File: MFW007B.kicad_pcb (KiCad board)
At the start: 4 copper layers, 84 x 42 mm, 98 parts, among them J1 Conn_01x04, J2 Conn_02x07, J3 4P JST-SH, J4 Conn_02x03, SW2 SW_Push, SW3 SW_Push, SW4 SW_Push, U1 24AA02-OT, U2 W5500, U3 STM32F103C8T6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

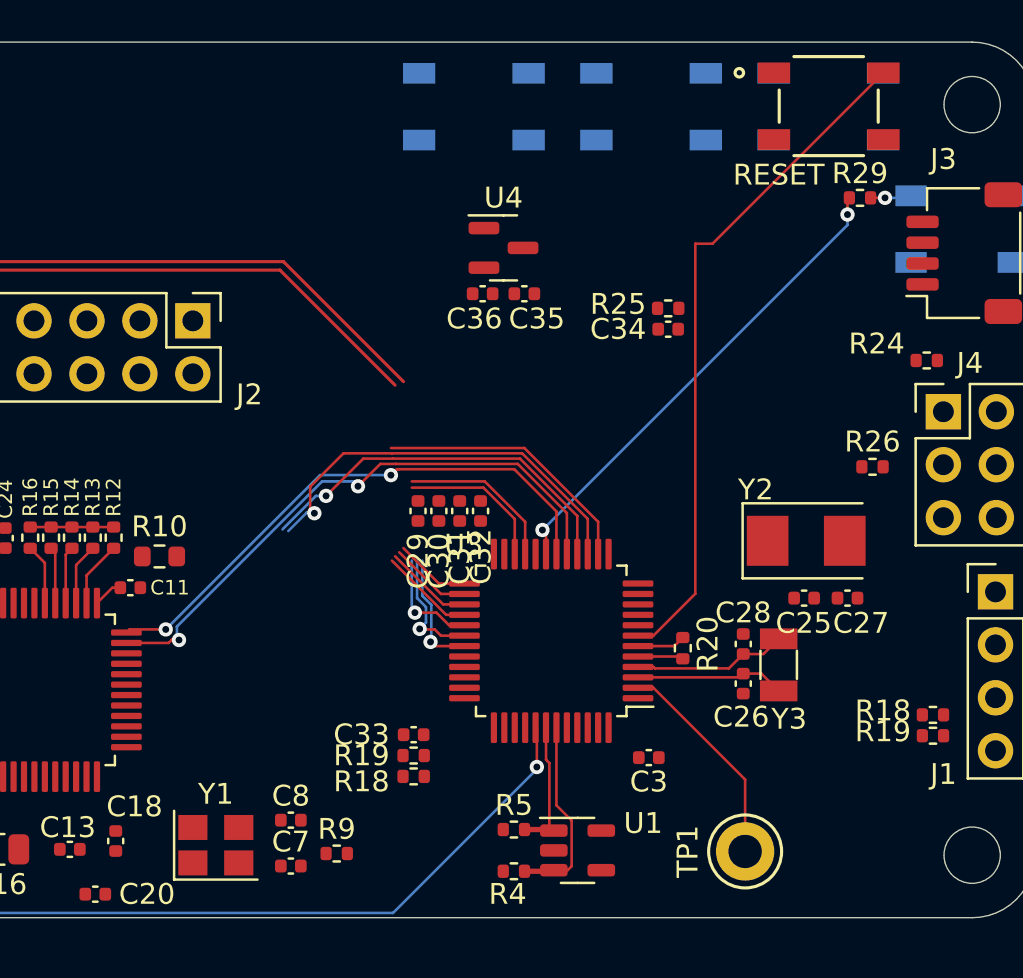
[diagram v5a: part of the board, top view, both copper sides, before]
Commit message: rotate mcu
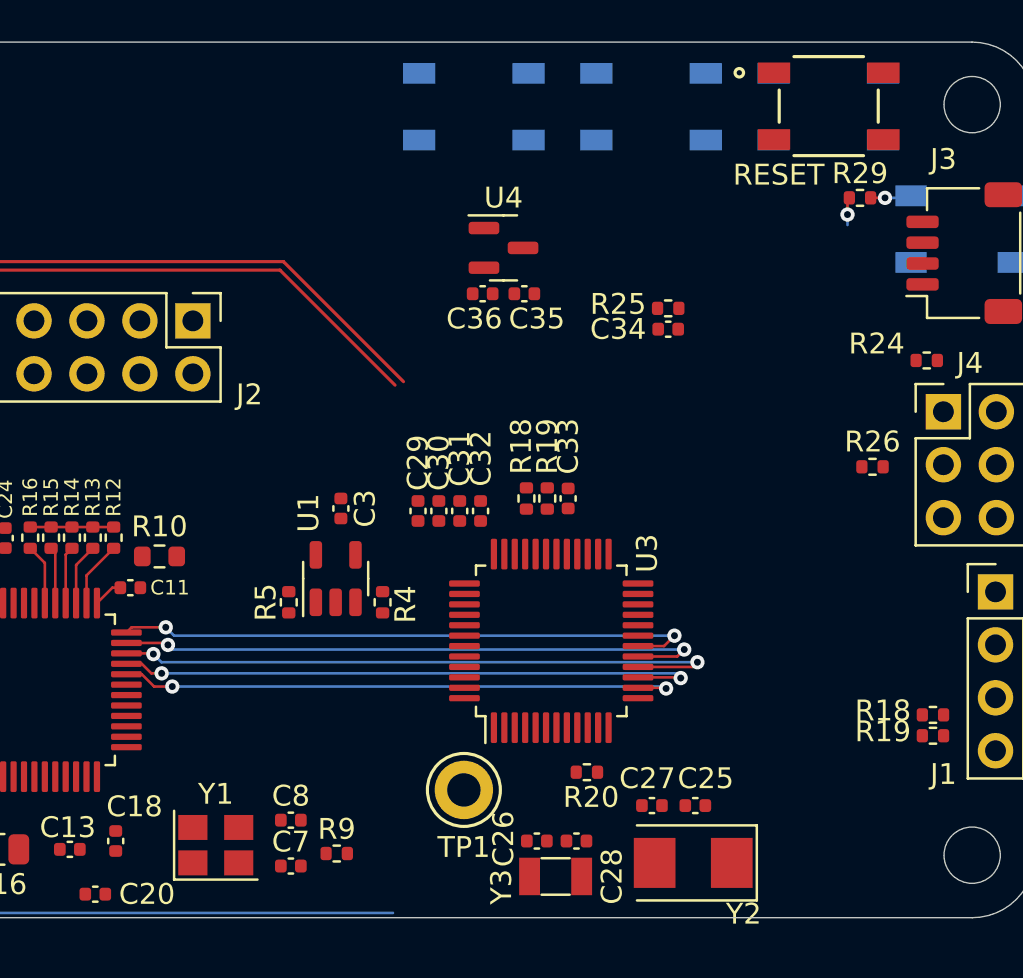
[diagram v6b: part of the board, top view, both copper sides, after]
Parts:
- moved C3 19.0 mm to (139.1, 101.5), turned to -90 degrees
- moved U1 17.5 mm to (138.8, 104.9), turned to 90 degrees
- moved Y2 16.4 mm to (156.0, 118.5), turned to 180 degrees
- moved R5 15.3 mm to (136.6, 106.0), turned to -90 degrees
- moved Y3 14.7 mm to (149.4, 119.2), turned to 0 degrees
- moved R18 14.4 mm to (148.0, 101.0), turned to 90 degrees
- moved R4 14.4 mm to (141.1, 106.0), turned to -90 degrees
- moved R19 13.9 mm to (149.0, 101.0), turned to -90 degrees
- moved TP1 13.8 mm to (145.0, 115.0), turned to 180 degrees
- moved C27 13.7 mm to (154.0, 115.8), turned to 180 degrees
- moved C33 13.5 mm to (150.0, 101.0), turned to -90 degrees
- moved C26 12.5 mm to (148.5, 117.5), turned to 180 degrees
- moved C28 12.4 mm to (150.4, 117.5), turned to 0 degrees
- moved C25 11.2 mm to (156.1, 115.8), turned to 180 degrees
- moved R20 7.52 mm to (150.9, 114.2), turned to 0 degrees
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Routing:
- net /RESET_SW: track 32.8 -> 0.00 mm
- net /RGB_LED: track 23.3 -> 1.34 mm, vias 2 -> 1
- net /Ethernet MAC PHY/CS: track 13.0 -> 27.5 mm, vias 0 -> 2
- net /Ethernet MAC PHY/MISO: track 18.5 -> 30.5 mm, vias 1 -> 2
- net /NTP_LED: track 61.3 -> 49.6 mm, vias 2 -> 1
- net Net-(TP1-Pad1): track 10.4 -> 0.00 mm
- net /I2C1_SDA: track 9.31 -> 0.00 mm
- net /Ethernet MAC PHY/SCLK: track 19.9 -> 28.9 mm, vias 1 -> 2
- net /I2C2_SCL: track 7.79 -> 0.00 mm
- net /MCU/OSC32_OUT: track 7.37 -> 0.00 mm
- net /I2C2_SDA: track 7.25 -> 0.00 mm
- net /MCU/OSC32_IN: track 7.17 -> 0.00 mm
- net /I2C1_SCL: track 6.52 -> 0.00 mm
- net /USER_SW_2: track 5.86 -> 0.00 mm, vias 1 -> 0
- net /USER_SW_3: track 5.80 -> 0.00 mm, vias 1 -> 0
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
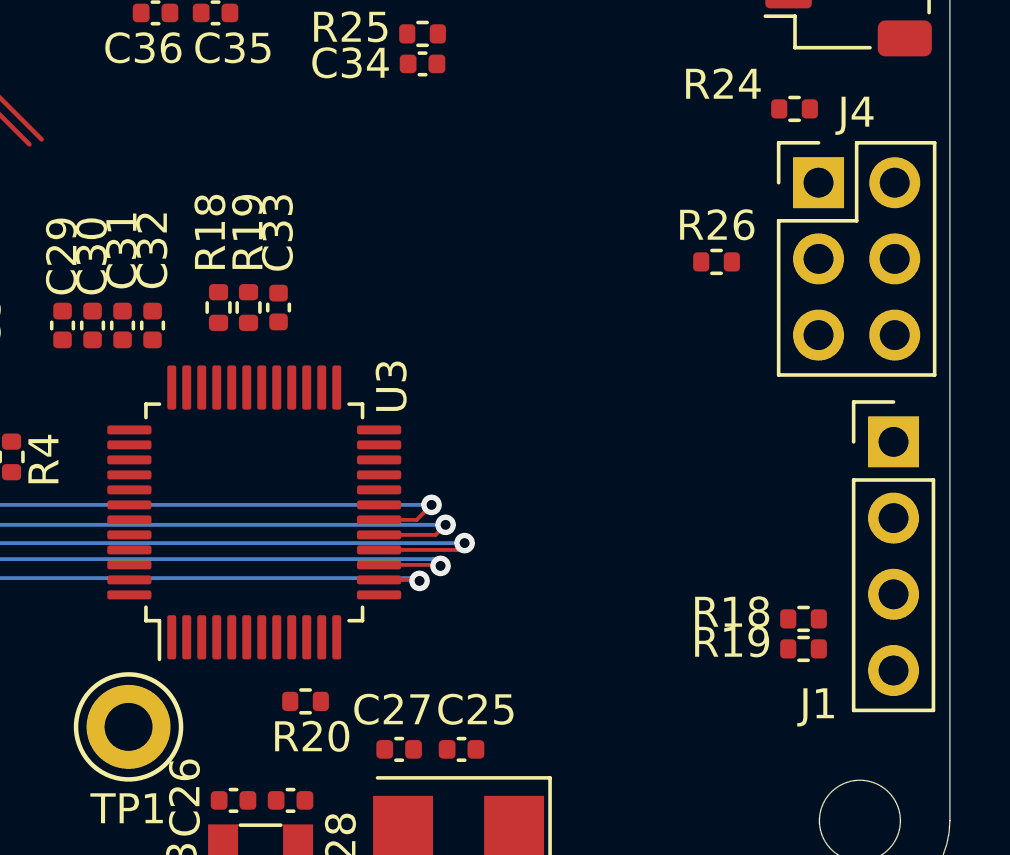
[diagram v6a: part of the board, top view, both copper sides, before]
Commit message: remove duplicate components
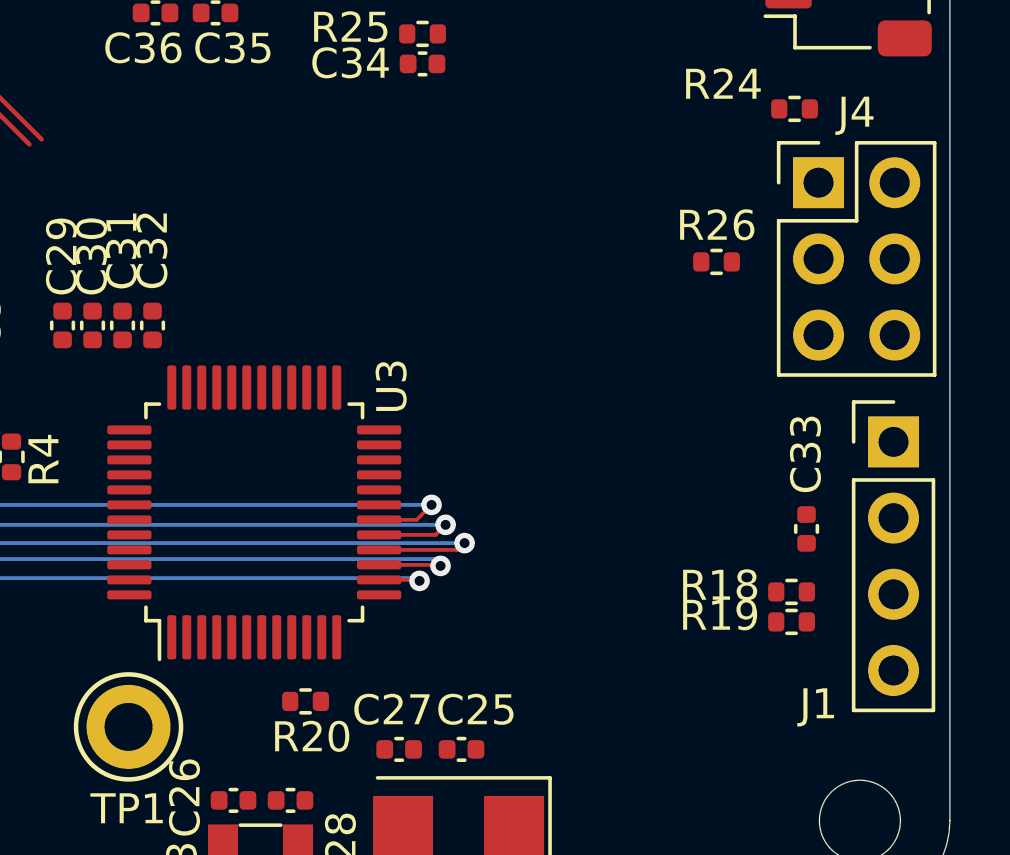
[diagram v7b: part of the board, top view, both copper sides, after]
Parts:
- removed the R18 at (148.0, 101.0)
- removed the R19 at (149.0, 101.0)
- moved C33 19.1 mm to (167.6, 108.4)
- moved R18 0.98 mm to (167.1, 110.5)
- moved R19 0.98 mm to (167.1, 111.5)
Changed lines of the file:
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@@
   )
   (footprint "Resistor_SMD:R_0402_1005Metric" (layer "F.Cu")
-    (at 167.5 111.4 180)
+    (at 167.1 110.5 180)
     (descr "Resistor SMD 0402 (1005 Metric), square (rectangular) end terminal, IPC_7351 nominal, (Body size source: IPC-SM-782 page 72, https://www.pcb-3d.com/wordpress/wp-content/uploads/ipc-sm-782a_amendment_1_and_2.pdf), generated with kicad-footprint-generator")
     (tags "resistor")
@@
   )
   (footprint "Capacitor_SMD:C_0402_1005Metric" (layer "F.Cu")
-    (at 150 101.02 -90)
+    (at 167.6 108.4 -90)
     (descr "Capacitor SMD 0402 (1005 Metric), square (rectangular) end terminal, IPC_7351 nominal, (Body size source: IPC-SM-782 page 76, https://www.pcb-3d.com/wordpress/wp-content/uploads/ipc-sm-782a_amendment_1_and_2.pdf), generated with kicad-footprint-generator")
     (tags "capacitor")
@@
     (pad "2" smd roundrect (at 0.51 0 180) (locked) (size 0.54 0.64) (layers "F.Cu" "F.Paste" "F.Mask") (roundrect_rratio 0.25)
       (net 74 "/MCU/BOOT1"))
-    (model "${KICAD6_3DMODEL_DIR}/Resistor_SMD.3dshapes/R_0402_1005Metric.wrl"
-      (offset (xyz 0 0 0))
-      (scale (xyz 1 1 1))
-      (rotate (xyz 0 0 0))
-    )
-  )
-  (footprint "Resistor_SMD:R_0402_1005Metric" (layer "F.Cu")
-    (at 149 101.02 -90)
-    (descr "Resistor SMD 0402 (1005 Metric), square (rectangular) end terminal, IPC_7351 nominal, (Body size source: IPC-SM-782 page 72, https://www.pcb-3d.com/wordpress/wp-content/uploads/ipc-sm-782a_amendment_1_and_2.pdf), generated with kicad-footprint-generator")
-    (tags "resistor")
-    (property "Sheet file" "mcu.kicad_sch")
-    (property "Sheet name" "MCU")
-    (attr smd)
-    (fp_text reference "R19" (at -2.5 0 90) (layer "F.SilkS")
-      (effects (font (size 1 1) (thickness 0.15)))
-    )
-    (fp_text value "10K" (at -2.25 1.25 90) (layer "F.Fab")
-      (effects (font (size 1 1) (thickness 0.15)))
-    )
-    (fp_text user "${REFERENCE}" (at 0 0 90) (layer "F.Fab")
-      (effects (font (size 0.26 0.26) (thickness 0.04)))
-    )
-    (fp_line (start -0.153641 0.38) (end 0.153641 0.38) (layer "F.SilkS") (width 0.12))
-    (fp_line (start -0.153641 -0.38) (end 0.153641 -0.38) (layer "F.SilkS") (width 0.12))
-    (fp_line (start 0.93 -0.47) (end 0.93 0.47) (layer "F.CrtYd") (width 0.05))
-    (fp_line (start 0.93 0.47) (end -0.93 0.47) (layer "F.CrtYd") (width 0.05))
-    (fp_line (start -0.93 -0.47) (end 0.93 -0.47) (layer "F.CrtYd") (width 0.05))
-    (fp_line (start -0.93 0.47) (end -0.93 -0.47) (layer "F.CrtYd") (width 0.05))
-    (fp_line (start 0.525 -0.27) (end 0.525 0.27) (layer "F.Fab") (width 0.1))
-    (fp_line (start 0.525 0.27) (end -0.525 0.27) (layer "F.Fab") (width 0.1))
-    (fp_line (start -0.525 -0.27) (end 0.525 -0.27) (layer "F.Fab") (width 0.1))
-    (fp_line (start -0.525 0.27) (end -0.525 -0.27) (layer "F.Fab") (width 0.1))
-    (pad "1" smd roundrect (at -0.51 0 270) (locked) (size 0.54 0.64) (layers "F.Cu" "F.Paste" "F.Mask") (roundrect_rratio 0.25)
-      (net 3 "+3V3"))
-    (pad "2" smd roundrect (at 0.51 0 270) (locked) (size 0.54 0.64) (layers "F.Cu" "F.Paste" "F.Mask") (roundrect_rratio 0.25)
-      (net 23 "/MCU/SWCLK"))
     (model "${KICAD6_3DMODEL_DIR}/Resistor_SMD.3dshapes/R_0402_1005Metric.wrl"
       (offset (xyz 0 0 0))
@@
     )
   )
-  (footprint "Resistor_SMD:R_0402_1005Metric" (layer "F.Cu")
-    (at 148 101.02 90)
-    (descr "Resistor SMD 0402 (1005 Metric), square (rectangular) end terminal, IPC_7351 nominal, (Body size source: IPC-SM-782 page 72, https://www.pcb-3d.com/wordpress/wp-content/uploads/ipc-sm-782a_amendment_1_and_2.pdf), generated with kicad-footprint-generator")
-    (tags "resistor")
-    (property "Sheet file" "mcu.kicad_sch")
-    (property "Sheet name" "MCU")
-    (attr smd)
-    (fp_text reference "R18" (at 2.5 -0.25 90) (layer "F.SilkS")
-      (effects (font (size 1 1) (thickness 0.15)))
-    )
-    (fp_text value "10K" (at 2.25 1 90) (layer "F.Fab")
-      (effects (font (size 1 1) (thickness 0.15)))
-    )
-    (fp_text user "${REFERENCE}" (at 0 0 90) (layer "F.Fab")
-      (effects (font (size 0.26 0.26) (thickness 0.04)))
-    )
-    (fp_line (start -0.153641 -0.38) (end 0.153641 -0.38) (layer "F.SilkS") (width 0.12))
-    (fp_line (start -0.153641 0.38) (end 0.153641 0.38) (layer "F.SilkS") (width 0.12))
-    (fp_line (start -0.93 0.47) (end -0.93 -0.47) (layer "F.CrtYd") (width 0.05))
-    (fp_line (start 0.93 -0.47) (end 0.93 0.47) (layer "F.CrtYd") (width 0.05))
-    (fp_line (start -0.93 -0.47) (end 0.93 -0.47) (layer "F.CrtYd") (width 0.05))
-    (fp_line (start 0.93 0.47) (end -0.93 0.47) (layer "F.CrtYd") (width 0.05))
-    (fp_line (start 0.525 0.27) (end -0.525 0.27) (layer "F.Fab") (width 0.1))
-    (fp_line (start -0.525 -0.27) (end 0.525 -0.27) (layer "F.Fab") (width 0.1))
-    (fp_line (start 0.525 -0.27) (end 0.525 0.27) (layer "F.Fab") (width 0.1))
-    (fp_line (start -0.525 0.27) (end -0.525 -0.27) (layer "F.Fab") (width 0.1))
-    (pad "1" smd roundrect (at -0.51 0 90) (locked) (size 0.54 0.64) (layers "F.Cu" "F.Paste" "F.Mask") (roundrect_rratio 0.25)
-      (net 24 "/MCU/SWO"))
-    (pad "2" smd roundrect (at 0.51 0 90) (locked) (size 0.54 0.64) (layers "F.Cu" "F.Paste" "F.Mask") (roundrect_rratio 0.25)
-      (net 1 "GND"))
-    (model "${KICAD6_3DMODEL_DIR}/Resistor_SMD.3dshapes/R_0402_1005Metric.wrl"
-      (offset (xyz 0 0 0))
-      (scale (xyz 1 1 1))
-      (rotate (xyz 0 0 0))
-    )
-  )
   (footprint "Capacitor_SMD:C_0402_1005Metric" (layer "F.Cu")
     (at 136.7 118.65)
@@
   )
   (footprint "Resistor_SMD:R_0402_1005Metric" (layer "F.Cu")
-    (at 167.5 112.4)
+    (at 167.1 111.5)
     (descr "Resistor SMD 0402 (1005 Metric), square (rectangular) end terminal, IPC_7351 nominal, (Body size source: IPC-SM-782 page 72, https://www.pcb-3d.com/wordpress/wp-content/uploads/ipc-sm-782a_amendment_1_and_2.pdf), generated with kicad-footprint-generator")
     (tags "resistor")

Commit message: more routing
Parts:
- moved R27 19.1 mm to (111.7, 118.3)
- moved R28 19.0 mm to (111.7, 117.2), turned to 180 degrees
- moved G*** 14.6 mm to (144.6, 98.0)
- moved R6 10.4 mm to (113.6, 108.8), turned to 90 degrees
- moved R8 8.88 mm to (113.6, 110.7)
- moved C4 8.48 mm to (112.6, 108.8)
- moved C6 8.07 mm to (114.5, 111.2), turned to 90 degrees
- moved R7 7.69 mm to (115.5, 106.2), turned to -90 degrees
- moved C5 6.82 mm to (112.6, 110.7), turned to -90 degrees
- moved R3 6.49 mm to (115.5, 108.1)
- moved R11 5.29 mm to (111.7, 113.9), turned to 180 degrees
- moved R9 5.05 mm to (136.7, 113.5)
- moved Y2 4.30 mm to (157.3, 114.4), turned to -90 degrees
- moved Y1 4.17 mm to (133.5, 113.5)
- moved C8 4.15 mm to (136.7, 112.3)
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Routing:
- net /RESET_SW: track 0.00 -> 42.1 mm
- net /MCU/SWCLK: track 0.00 -> 32.4 mm, vias 0 -> 2
- net /MCU/SWO: track 0.00 -> 27.7 mm, vias 0 -> 2
- net /MCU/BOOT0: track 0.00 -> 27.5 mm, vias 0 -> 2
- net /ETHLINKLED: track 0.00 -> 21.4 mm, vias 0 -> 2
- net /ETHACTLED: track 0.00 -> 19.2 mm, vias 0 -> 2
- net /TDP: track 0.00 -> 16.4 mm, vias 0 -> 1
- net /NTP_LED: track 49.6 -> 65.2 mm, vias 1 -> 2
- net /TDN: track 0.00 -> 14.7 mm, vias 0 -> 1
- net /MCU/BOOT1: track 0.00 -> 14.2 mm, vias 0 -> 2
- net Net-(C7-Pad1): track 0.00 -> 11.8 mm
- net /MCU/OSC_OUT: track 0.00 -> 11.7 mm, vias 0 -> 2
- net /MCU/OSC_IN: track 0.00 -> 11.7 mm
- net Net-(C8-Pad1): track 0.00 -> 11.6 mm
- net /CD: track 0.00 -> 11.5 mm
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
